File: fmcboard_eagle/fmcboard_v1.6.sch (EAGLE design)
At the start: 239 parts, among them IC1 OPA695IDR, IC10 LM358, IC11 7805DT, IC12 SN74AUC2G66DCTR, IC13 SN74AUC2G66DCTR, IC14 SN74AUC2G66DCTR, IC15 SN74AUC2G66DCTR, IC16 DAC7578SPWR, IC17 SN74AUC2G66DCTR, IC18 SN74AUC2G66DCTR, IC19 SN74AUC2G66DCTR, IC2 DAC7578SPWR, IC20 SN74AUC2G66DCTR, IC21 74AUP2GU04GW, IC22 74AUP2GU04GW, IC23 74AUP2GU04GW, IC24 74AUP2GU04GW, IC25 MC7905ACD2TR4G, IC26 AMS1117-1.8, IC27 OPA699ID, IC29 LM337KVURG3, IC3 LTC6229IMS8E#TRPBF, IC4 OPA695IDR, IC5 LTC6229IMS8E#TRPBF, IC6 OPA695IDR, IC7 OPA699ID, IC8 LM358, IC9 LM358, J1 8pin, J11 4p-2.54, J12 4p-2.54, J13 4p-2.54, J14 4p-2.54, J2 ASP-134604-01, J3 4p-2.54, J4 4p-2.54, J5 4p-2.54, J6 4p-2.54, J7 4p-2.54, J8 4p-2.54, J9 8pin, U1 TXS0108EPWR

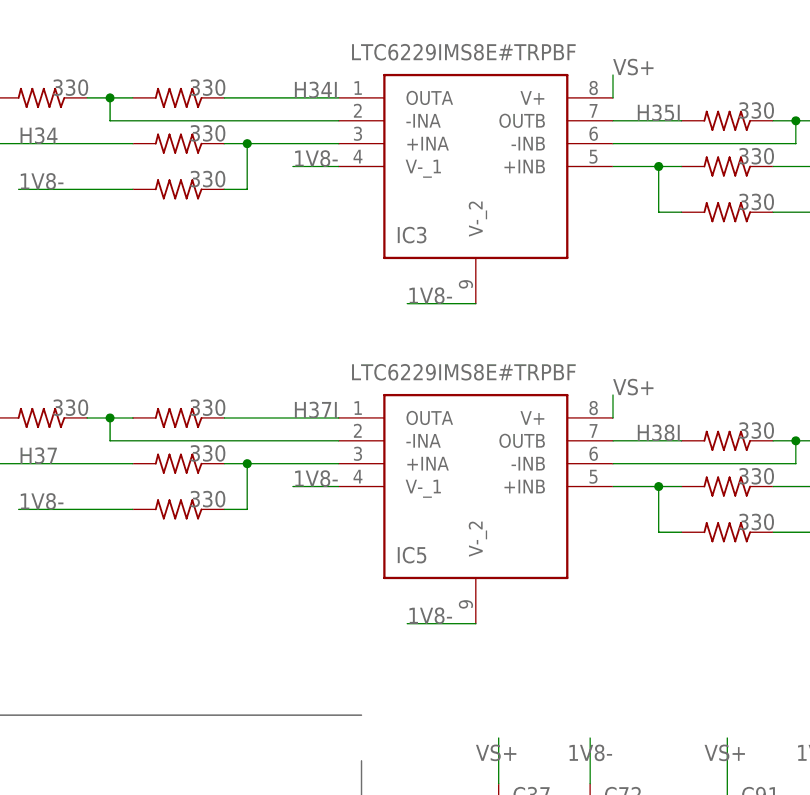
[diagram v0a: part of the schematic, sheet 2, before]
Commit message: Better 7805 7905 footprints
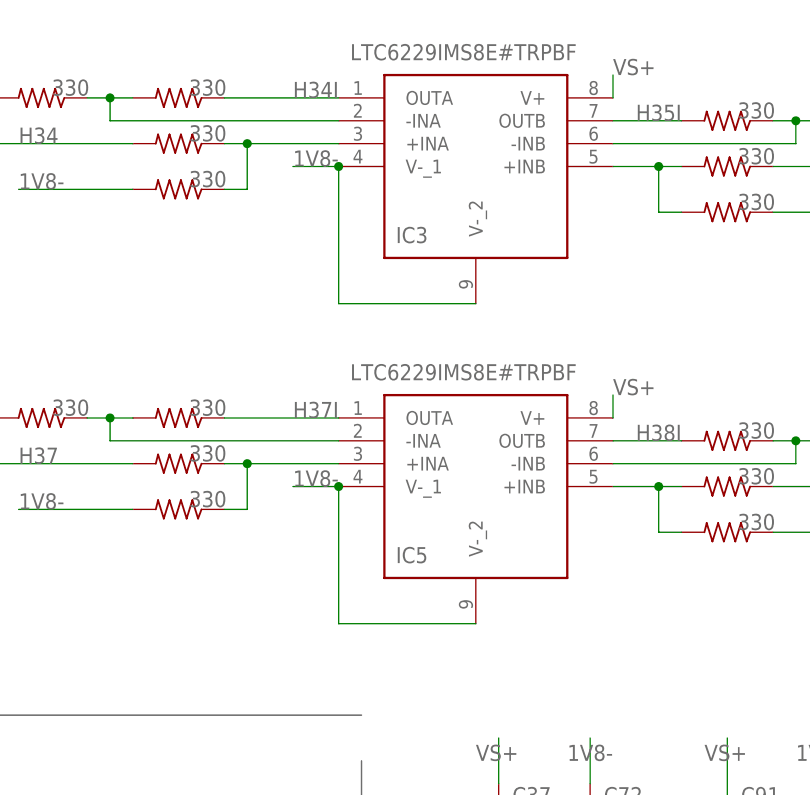
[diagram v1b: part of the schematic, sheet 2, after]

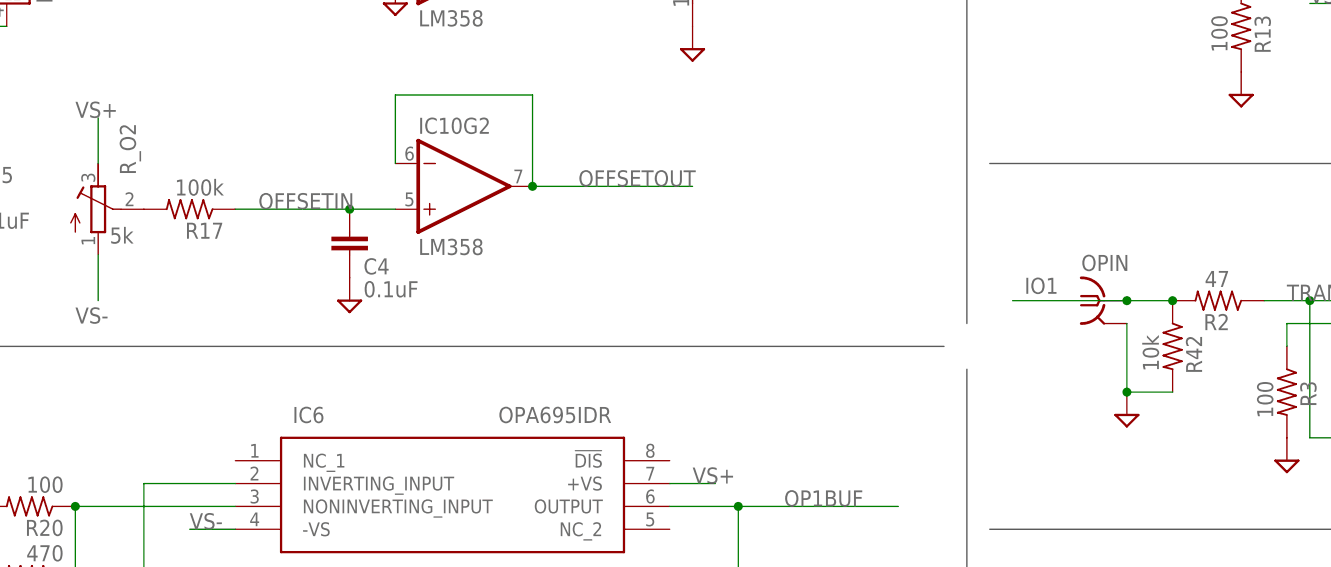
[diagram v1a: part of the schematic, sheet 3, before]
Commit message: mostly routed
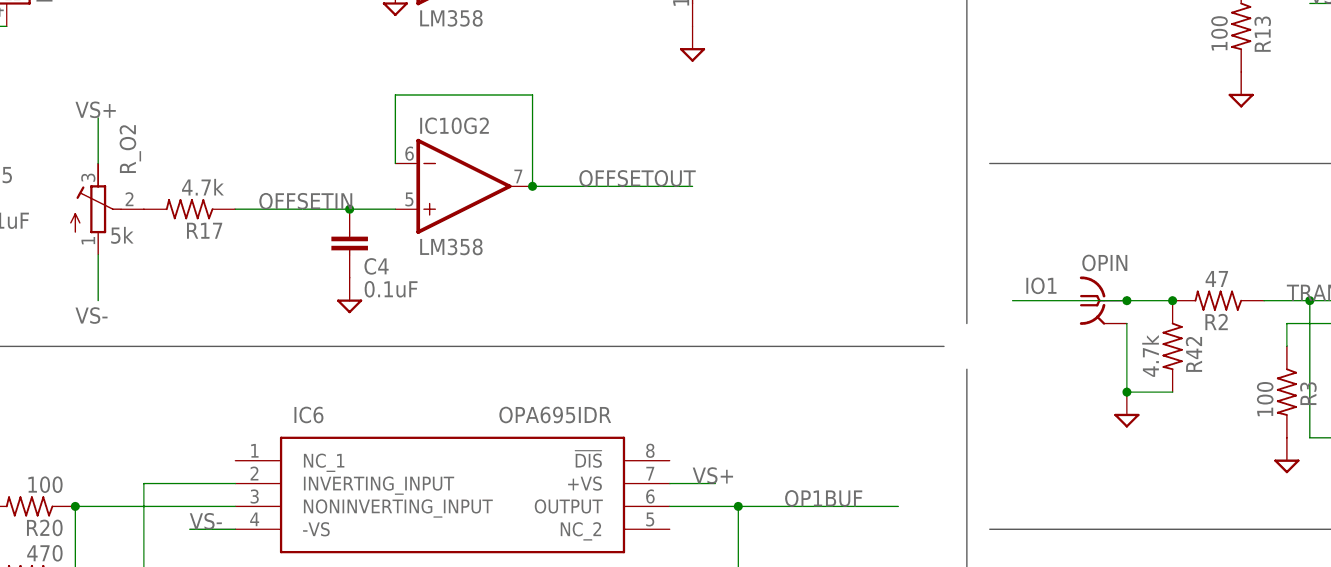
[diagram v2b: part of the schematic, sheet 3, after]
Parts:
- R17: value 100k -> 4.7k
- R42: value 10k -> 4.7k
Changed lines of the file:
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@@
 <part name="SUPPLY6" library="supply2" library_urn="urn:adsk.eagle:library:372" deviceset="GND" device=""/>
 <part name="R_O2" library="resistor" library_urn="urn:adsk.eagle:library:348" deviceset="R-TRIMM" device="3296W" package3d_urn="urn:adsk.eagle:package:26033/1" value="5k"/>
-<part name="R17" library="rcl" library_urn="urn:adsk.eagle:library:334" deviceset="R-US_" device="R0805" package3d_urn="urn:adsk.eagle:package:23553/2" value="100k"/>
+<part name="R17" library="rcl" library_urn="urn:adsk.eagle:library:334" deviceset="R-US_" device="R0805" package3d_urn="urn:adsk.eagle:package:23553/2" value="4.7k"/>
 <part name="SUPPLY29" library="supply2" library_urn="urn:adsk.eagle:library:372" deviceset="GND" device=""/>
 <part name="R18" library="rcl" library_urn="urn:adsk.eagle:library:334" deviceset="R-US_" device="R0805" package3d_urn="urn:adsk.eagle:package:23553/2" value="470"/>
@@
 <part name="R2" library="rcl" library_urn="urn:adsk.eagle:library:334" deviceset="R-US_" device="R0805" package3d_urn="urn:adsk.eagle:package:23553/2" value="47"/>
 <part name="R34" library="rcl" library_urn="urn:adsk.eagle:library:334" deviceset="R-US_" device="R0805" package3d_urn="urn:adsk.eagle:package:23553/2" value="47"/>
-<part name="R42" library="rcl" library_urn="urn:adsk.eagle:library:334" deviceset="R-US_" device="R0805" package3d_urn="urn:adsk.eagle:package:23553/2" value="10k"/>
+<part name="R42" library="rcl" library_urn="urn:adsk.eagle:library:334" deviceset="R-US_" device="R0805" package3d_urn="urn:adsk.eagle:package:23553/2" value="4.7k"/>
 <part name="J8" library="Seeed-Connector" library_urn="urn:adsk.eagle:library:478" deviceset="DIP-BLACK-FEMALE-HEADER-VERT(4P-2.54)" device="" package3d_urn="urn:adsk.eagle:package:33137/1" value="4p-2.54"/>
 <part name="SUPPLY30" library="supply2" library_urn="urn:adsk.eagle:library:372" deviceset="GND" device=""/>

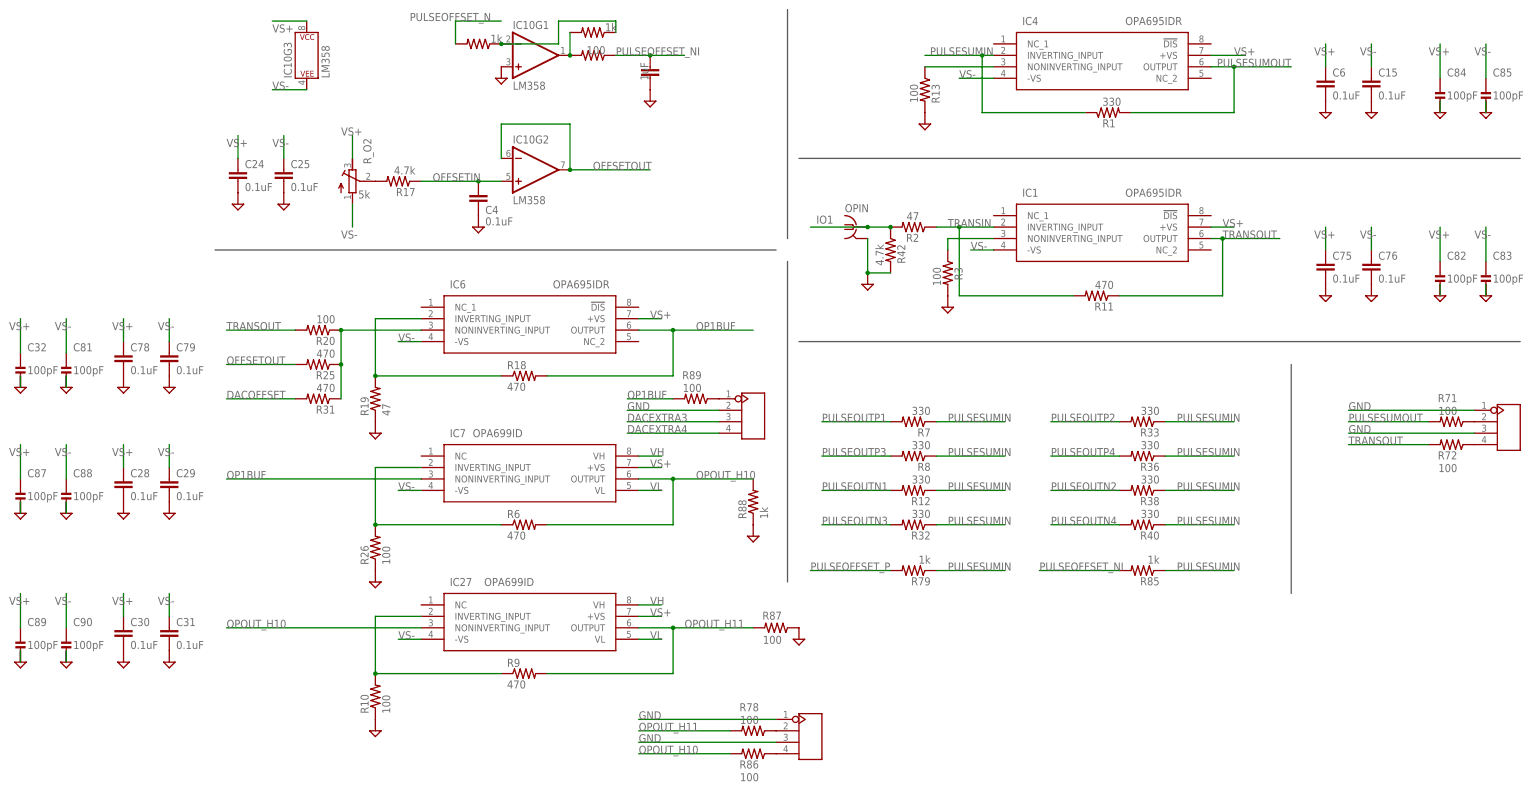
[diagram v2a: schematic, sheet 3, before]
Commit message: -1.8V 100uF cap for stability 330 -> 470 for 695 pulseout 330 -> 470 for inputs to pulseout Replace initial 695 with 699 for lower noise, and feedback 470 to 1k Increase gain for opbuf and h10, 470 -> 1k Remove h11 100 -> 10 ohm before h10 h11 pulseout probe points
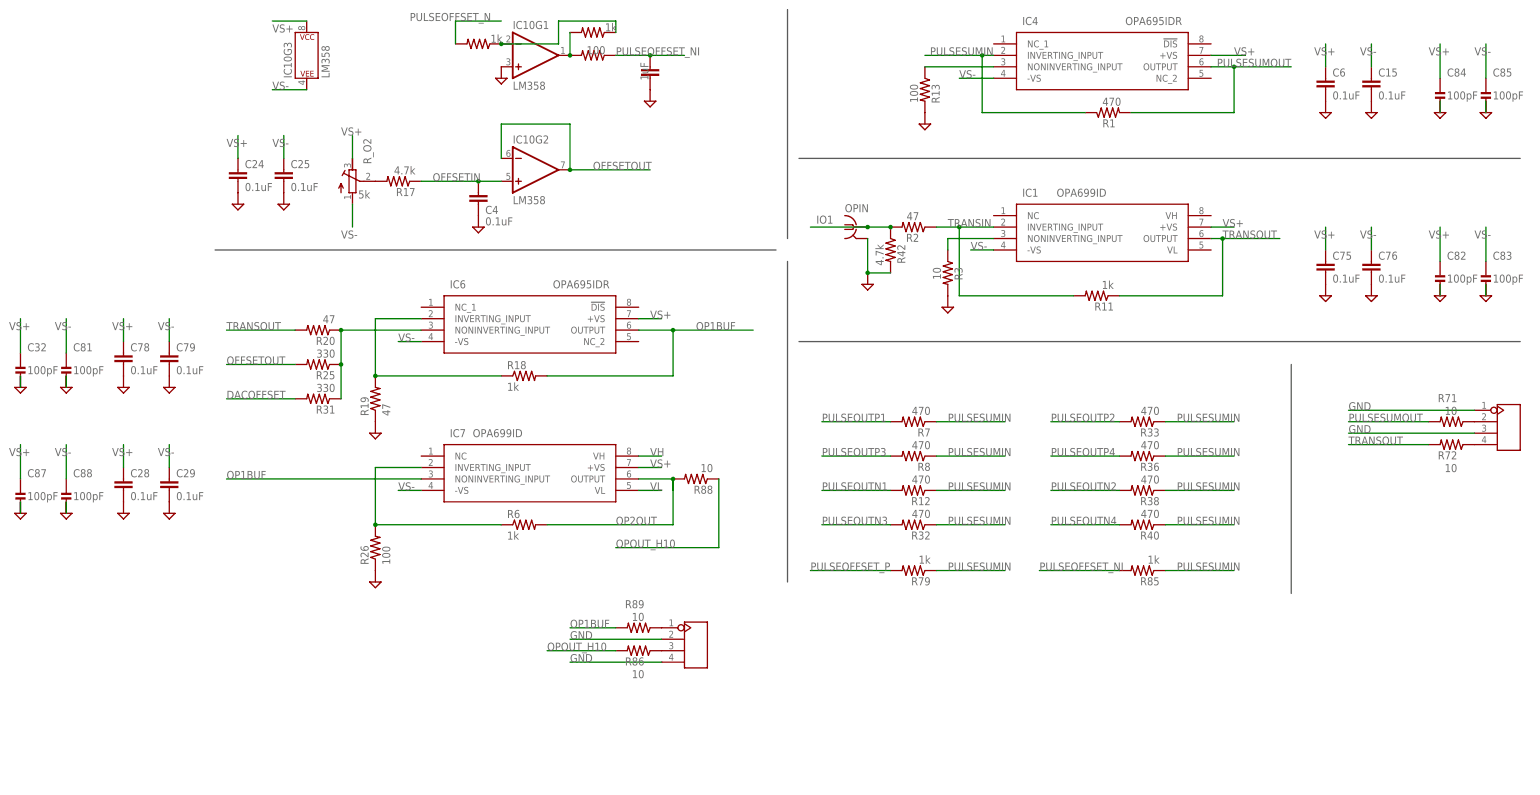
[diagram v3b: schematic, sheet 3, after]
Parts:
- removed C30, C31: 0.1uF, SparkFun-Passives:CAP0805
- removed C89, C90: 100pF, passives:CAPACITOR0603_CAP
- removed IC27: OPA699ID, OPA699ID:OPA699ID
- removed J14: 4p-2.54, Seeed-Connector:DIP-BLACK-FEMALE-HEADER-VERT(4P-2.54)
- removed R10, R78, R87: 100, rcl:R-US_R0805
- removed R9: 470, rcl:R-US_R0805
- added C95: 100uF, SparkFun-Passives:CAP_POLSMD
- IC1: value OPA695IDR -> OPA699ID; device OPA695IDR:OPA695IDR -> OPA699ID:OPA699ID
- R1, R12, R32, R33, R36, R38, R40, R7, R8: value 330 -> 470
- R11, R18, R6: value 470 -> 1k
- R20: value 100 -> 47
- R25, R31: value 470 -> 330
- R3, R71, R72, R86, R89: value 100 -> 10
- R88: value 1k -> 10
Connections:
- removed net DACEXTRA3: IC16.VOUTD, J5.P$3
- removed net DACEXTRA4: IC16.VOUTE, J5.P$4
- removed net N$1: IC27.INVERTING_INPUT, R10.2, R9.1
- removed net N$41: J14.P$4, R86.1
- new net OP2OUT: IC7.OUTPUT, R6.2, R88.2
- net 1V8-: now also C95.-
- net GND: now also C95.+, J5.P$4; no longer C30.2, C31.2, C89.2, C90.2, J14.P$1, J14.P$3, R10.1, R87.1, R88.1
- net N$40: now also J5.P$3, R86.1; no longer J14.P$2, R78.1
- net OPOUT_H10: now also R88.1; no longer IC27.NONINVERTING_INPUT, IC7.OUTPUT, R6.2, R88.2
- net OPOUT_H11: no longer IC27.OUTPUT, R78.2, R87.2, R9.2
- net VH: no longer IC27.VH
- net VL: no longer IC27.VL
- net VS+: no longer C30.1, C89.1, IC27.+VS
- net VS-: no longer C31.1, C90.1, IC27.-VS
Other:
- moved on the sheet: C33, C65, C77, C86, IC29, R14, R70, R86, R88, R89

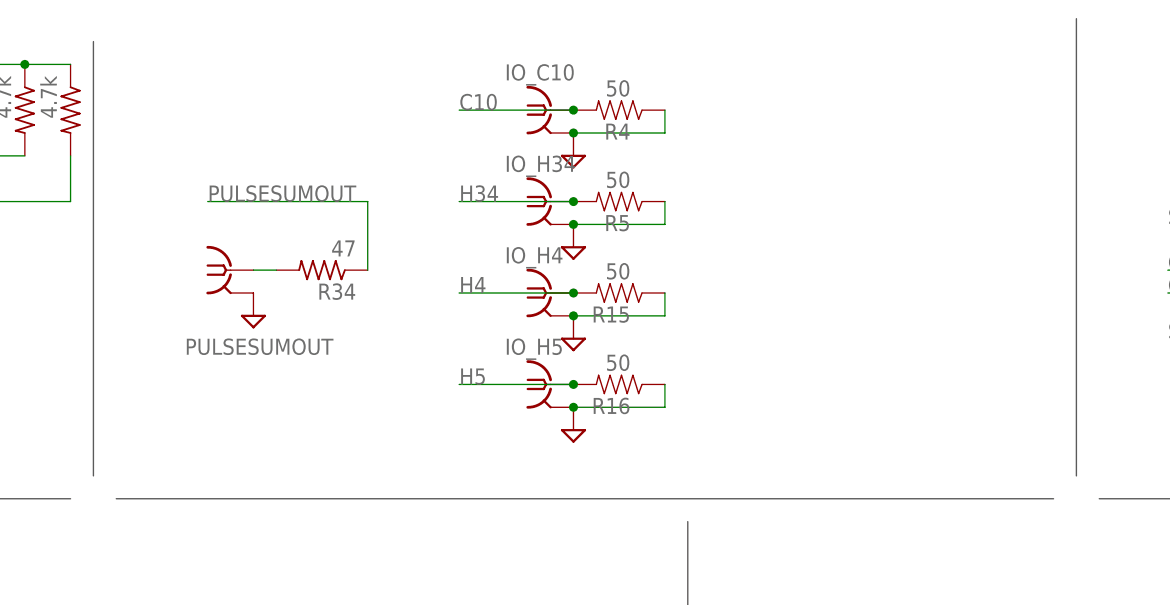
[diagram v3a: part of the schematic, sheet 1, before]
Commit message: v1.64 add test 2.6k resistor routed, better gnd connections
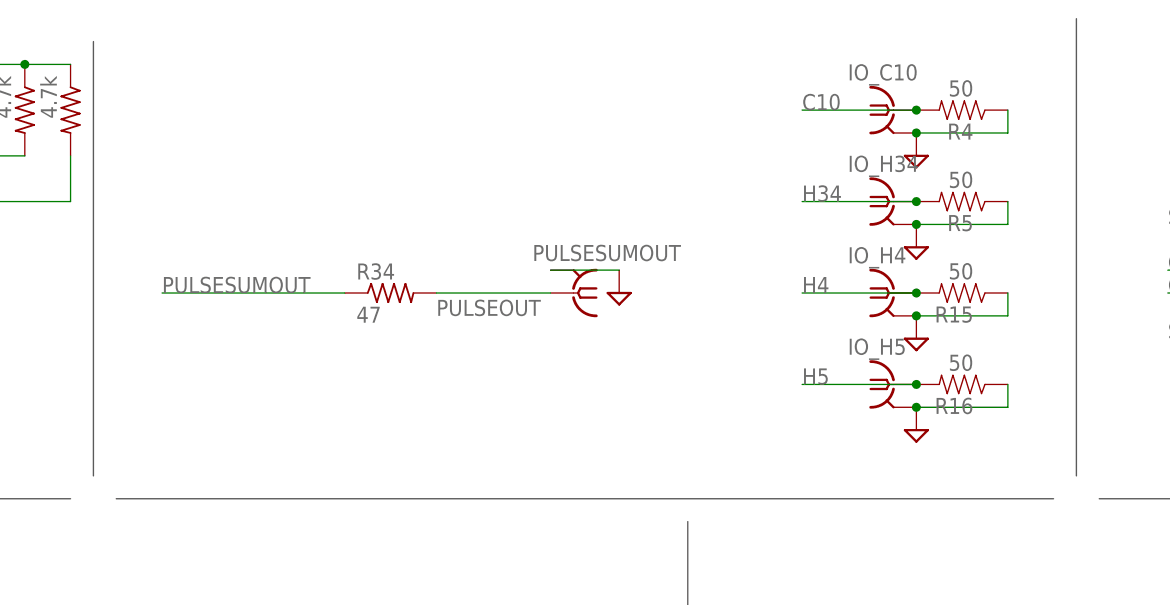
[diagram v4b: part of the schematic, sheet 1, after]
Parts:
- added R9: 2.6k, SparkFun-Resistors:RESISTORAXIAL-0.3
- R13: value 100 -> 10
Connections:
- removed net N$18: PULSESUMOUT.1, R34.2
- new net PULSEOUT: PULSESUMOUT.1, R34.2, R9.2
- net IO1: now also R9.1
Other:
- note added: "For testing"
- moved on the sheet: IO_C10, IO_H34, IO_H4, IO_H5, PULSESUMOUT, R15, R16, R34, R4, R5, R86, R89
